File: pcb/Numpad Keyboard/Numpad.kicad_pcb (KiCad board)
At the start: 2 copper layers, 82.4 x 128 mm, 57 parts, among them U1 MCP23S17_SO, U2 IS31FL3743-QF

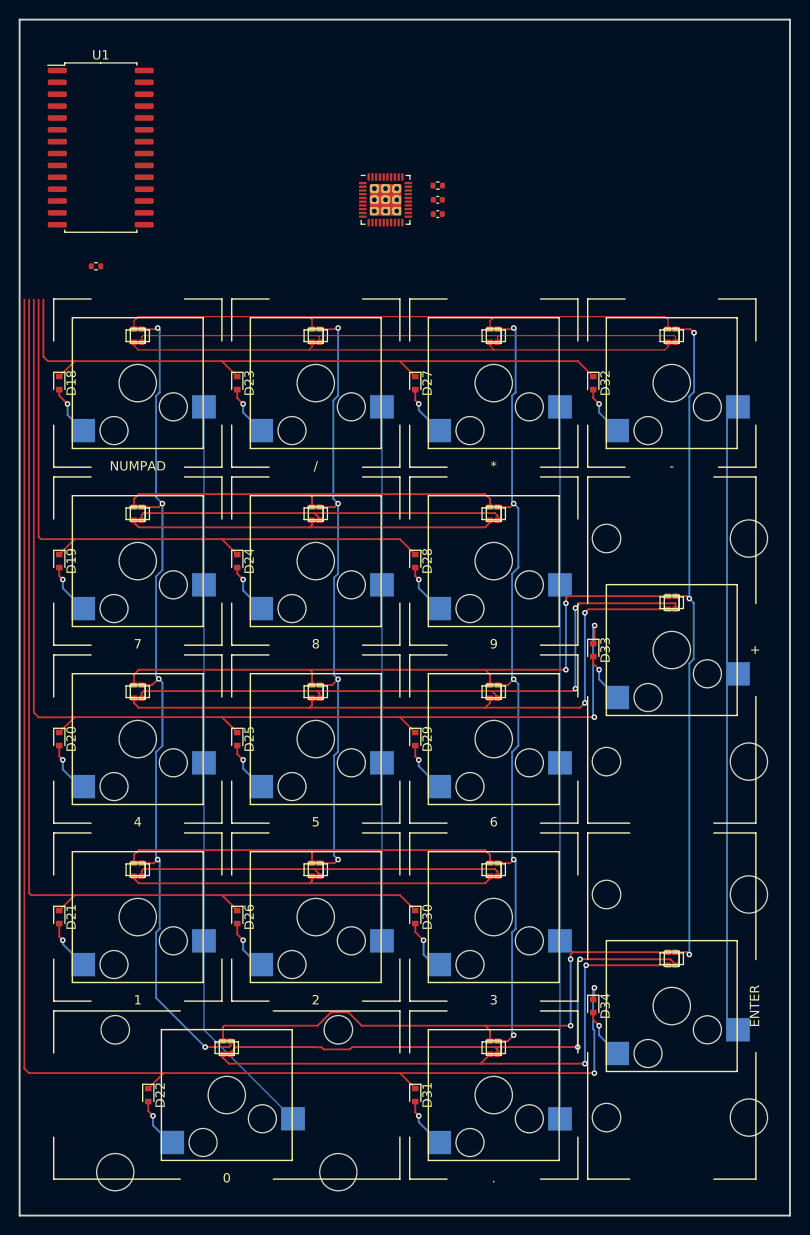
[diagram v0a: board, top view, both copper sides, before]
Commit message: Added second LED controller for higher current per LED
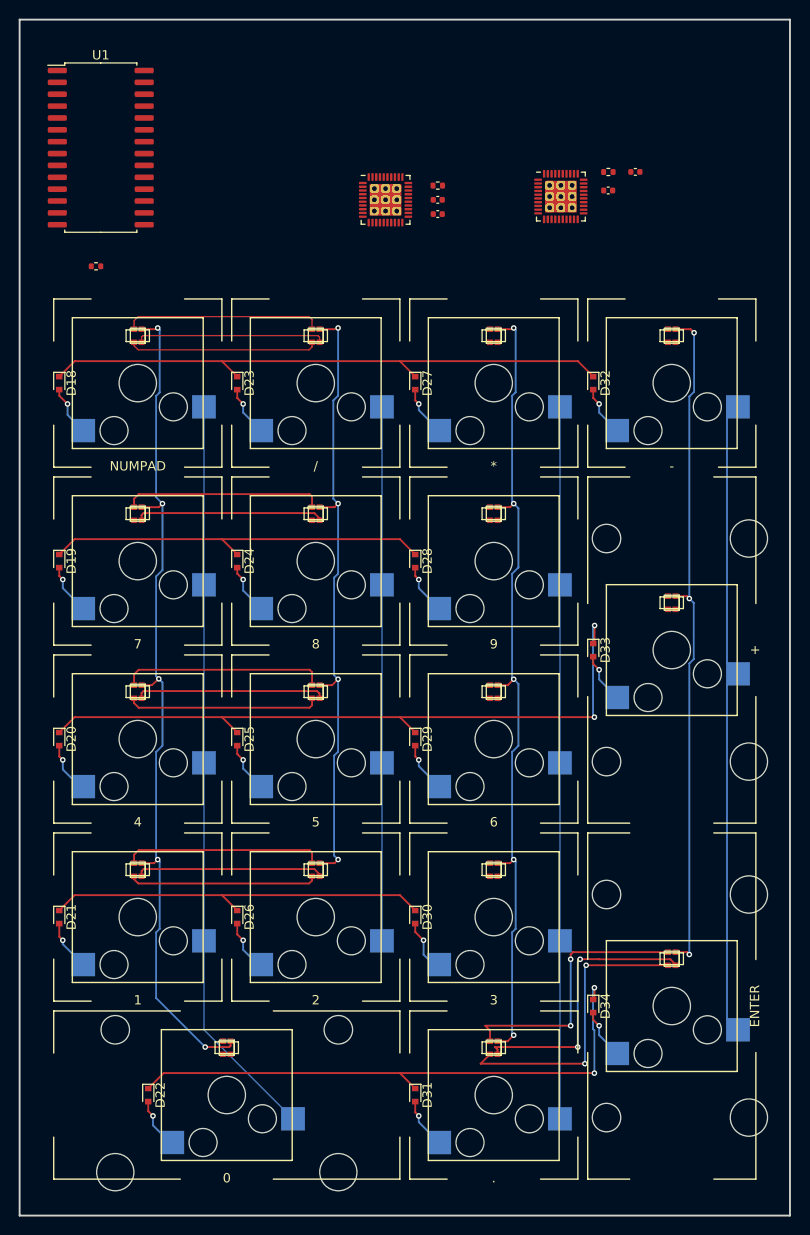
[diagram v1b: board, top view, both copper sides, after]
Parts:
- added C3: C 1uF, Footprints:C_0402_1005Metric, F.Cu at (84.8, 41.1)
- added C4: C_100nF, Footprints:C_0402_1005Metric, F.Cu at (87.7, 39.2)
- added R3: R, Footprints:R_0402_1005Metric, F.Cu at (84.9, 39.2)
- added U3: IS31FL3743-QF, Footprints:QFN-40-1EP_5x5mm_P0.4mm_EP3.4x3.4mm, F.Cu at (79.8, 41.8)
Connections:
- C1 pad 1: Net-(C1-Pad1) -> Net-(R1-Pad1)
- C1 pad 2: Net-(C1-Pad2) -> Net-(R2-Pad1)
- C2 pad 1: Net-(C1-Pad1) -> Net-(R1-Pad1)
- C2 pad 2: Net-(C1-Pad2) -> Net-(R2-Pad1)
- D10 pad 1: Net-(D1-Pad1) -> Net-(D10-Pad1)
- D10 pad 2: Net-(D1-Pad2) -> Net-(D10-Pad2)
- D10 pad 4: Net-(D1-Pad4) -> Net-(D10-Pad4)
- D14 pad 2: Net-(D14-Pad2) -> Net-(D17-Pad2)
- D15 pad 1: Net-(D1-Pad1) -> Net-(D10-Pad1)
- D15 pad 2: Net-(D1-Pad2) -> Net-(D10-Pad2)
- D15 pad 4: Net-(D1-Pad4) -> Net-(D10-Pad4)
- D17 pad 2: Net-(D14-Pad2) -> Net-(D17-Pad2)
- D2 pad 1: Net-(D11-Pad1) -> Net-(D2-Pad1)
- D2 pad 2: Net-(D11-Pad2) -> Net-(D2-Pad2)
- D2 pad 4: Net-(D11-Pad4) -> Net-(D2-Pad4)
- D3 pad 1: Net-(D12-Pad1) -> Net-(D3-Pad1)
- D3 pad 2: Net-(D12-Pad2) -> Net-(D3-Pad2)
- D3 pad 4: Net-(D12-Pad4) -> Net-(D3-Pad4)
- D4 pad 1: Net-(D13-Pad1) -> Net-(D4-Pad1)
- D4 pad 2: Net-(D13-Pad2) -> Net-(D4-Pad2)
- D4 pad 4: Net-(D13-Pad4) -> Net-(D4-Pad4)
- D5 pad 1: Net-(D14-Pad1) -> Net-(D5-Pad1)
- D5 pad 2: Net-(D14-Pad2) -> Net-(D5-Pad2)
- D5 pad 4: Net-(D14-Pad4) -> Net-(D5-Pad4)
- D7 pad 1: Net-(D11-Pad1) -> Net-(D2-Pad1)
- D7 pad 2: Net-(D11-Pad2) -> Net-(D2-Pad2)
- D7 pad 4: Net-(D11-Pad4) -> Net-(D2-Pad4)
- D8 pad 1: Net-(D12-Pad1) -> Net-(D3-Pad1)
- D8 pad 2: Net-(D12-Pad2) -> Net-(D3-Pad2)
- D8 pad 4: Net-(D12-Pad4) -> Net-(D3-Pad4)
- D9 pad 1: Net-(D13-Pad1) -> Net-(D4-Pad1)
- D9 pad 2: Net-(D13-Pad2) -> Net-(D4-Pad2)
- D9 pad 4: Net-(D13-Pad4) -> Net-(D4-Pad4)
- R1 pad 1: Net-(C1-Pad2) -> Net-(R1-Pad1)
- R2 pad 1: Net-(C1-Pad1) -> Net-(R2-Pad1)
- U1 pad 10: Net-(C1-Pad1) -> Net-(R2-Pad1)
- U1 pad 15: Net-(C1-Pad1) -> Net-(R2-Pad1)
- U1 pad 16: Net-(C1-Pad2) -> Net-(R1-Pad1)
- U1 pad 17: Net-(C1-Pad2) -> Net-(R1-Pad1)
- U1 pad 9: Net-(C1-Pad2) -> Net-(R1-Pad1)
- U2 pad 15: Net-(D14-Pad1) -> Net-(D5-Pad1)
- U2 pad 16: Net-(C1-Pad1) -> Net-(R2-Pad1)
- U2 pad 17: Net-(D14-Pad2) -> Net-(D5-Pad2)
- U2 pad 18: Net-(D14-Pad4) -> Net-(D5-Pad4)
- U2 pad 19: Net-(D13-Pad1) -> Net-(D4-Pad1)
- U2 pad 20: Net-(D13-Pad2) -> Net-(D4-Pad2)
- U2 pad 21: Net-(D13-Pad4) -> Net-(D4-Pad4)
- U2 pad 22: Net-(C1-Pad2) -> Net-(R1-Pad1)
- U2 pad 23: Net-(C1-Pad1) -> Net-(R2-Pad1)
- U2 pad 24: Net-(C1-Pad2) -> Net-(R1-Pad1)
- U2 pad 25: Net-(C1-Pad2) -> Net-(R1-Pad1)
- U2 pad 26: Net-(C1-Pad2) -> Net-(R1-Pad1)
- U2 pad 3: Net-(D15-Pad3) -> unconnected-(U2-Pad3)
- U2 pad 31: Net-(D12-Pad1) -> Net-(D3-Pad1)
- U2 pad 32: Net-(D12-Pad2) -> Net-(D3-Pad2)
- U2 pad 33: Net-(D12-Pad4) -> Net-(D3-Pad4)
- U2 pad 34: Net-(D11-Pad1) -> Net-(D2-Pad1)
- U2 pad 35: Net-(D11-Pad2) -> Net-(D2-Pad2)
- U2 pad 36: Net-(D11-Pad4) -> Net-(D2-Pad4)
- U2 pad 5: Net-(C1-Pad2) -> Net-(R1-Pad1)
- U2 pad 7: Net-(D10-Pad3) -> unconnected-(U2-Pad7)
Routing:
- net Net-(D22-Pad1): track 158.7 -> 61.2 mm
- net Net-(D12-Pad2): track 70.2 -> 0.00 mm, vias 2 -> 0
- net Net-(D12-Pad1): track 69.9 -> 0.00 mm, vias 2 -> 0
- net Net-(D12-Pad4): track 69.3 -> 0.00 mm, vias 2 -> 0
- net Net-(D21-Pad1): track 110.3 -> 41.8 mm
- net Net-(D14-Pad2): track 60.1 -> 0.00 mm, vias 2 -> 0
- net Net-(D20-Pad1): track 123.5 -> 74.3 mm
- net Net-(D11-Pad1): track 41.8 -> 0.00 mm
- net Net-(D13-Pad1): track 41.8 -> 0.00 mm
- net Net-(D1-Pad1): track 62.4 -> 21.3 mm
- net Net-(D13-Pad4): track 40.4 -> 0.00 mm
- net Net-(D11-Pad4): track 40.4 -> 0.00 mm
- net Net-(D1-Pad2): track 60.3 -> 20.2 mm
- net Net-(D11-Pad2): track 39.9 -> 0.00 mm
- net Net-(D13-Pad2): track 39.9 -> 0.00 mm
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
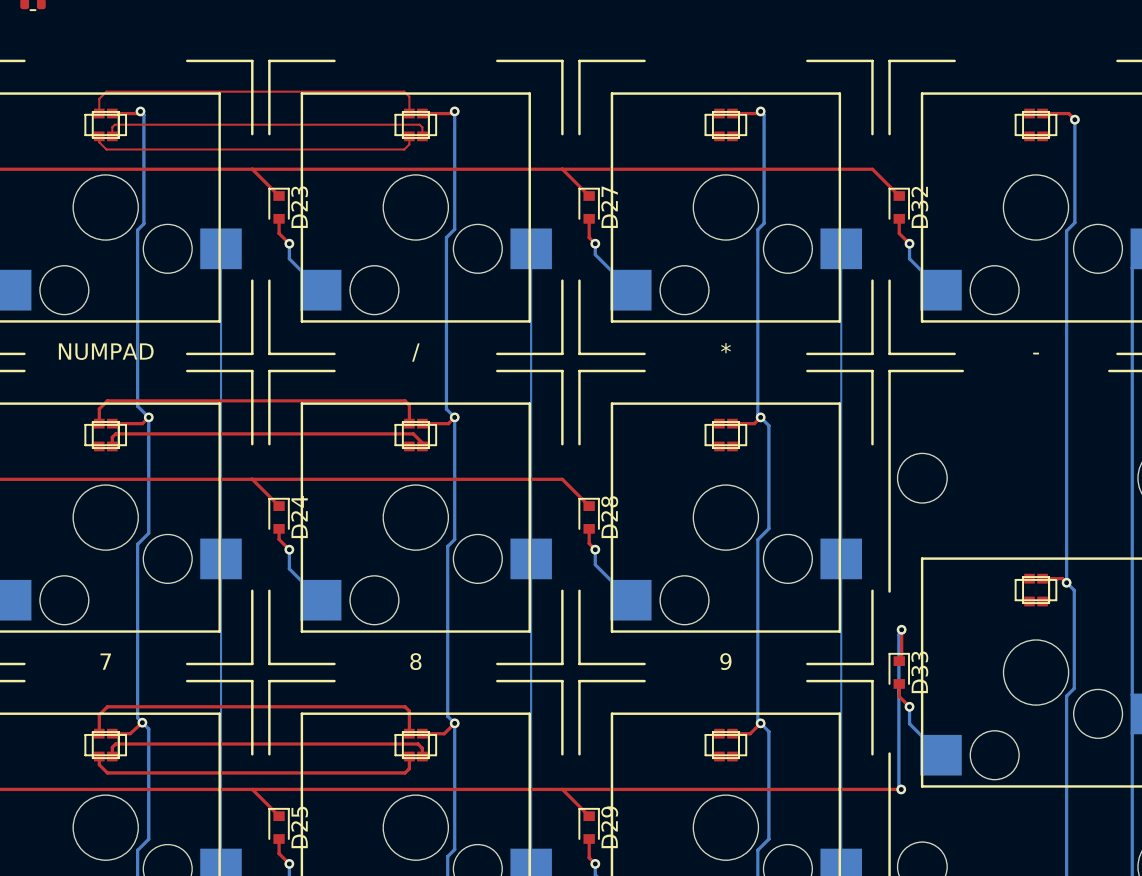
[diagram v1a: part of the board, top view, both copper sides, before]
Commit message: Removed several capacitors to decrease current consumption on startup
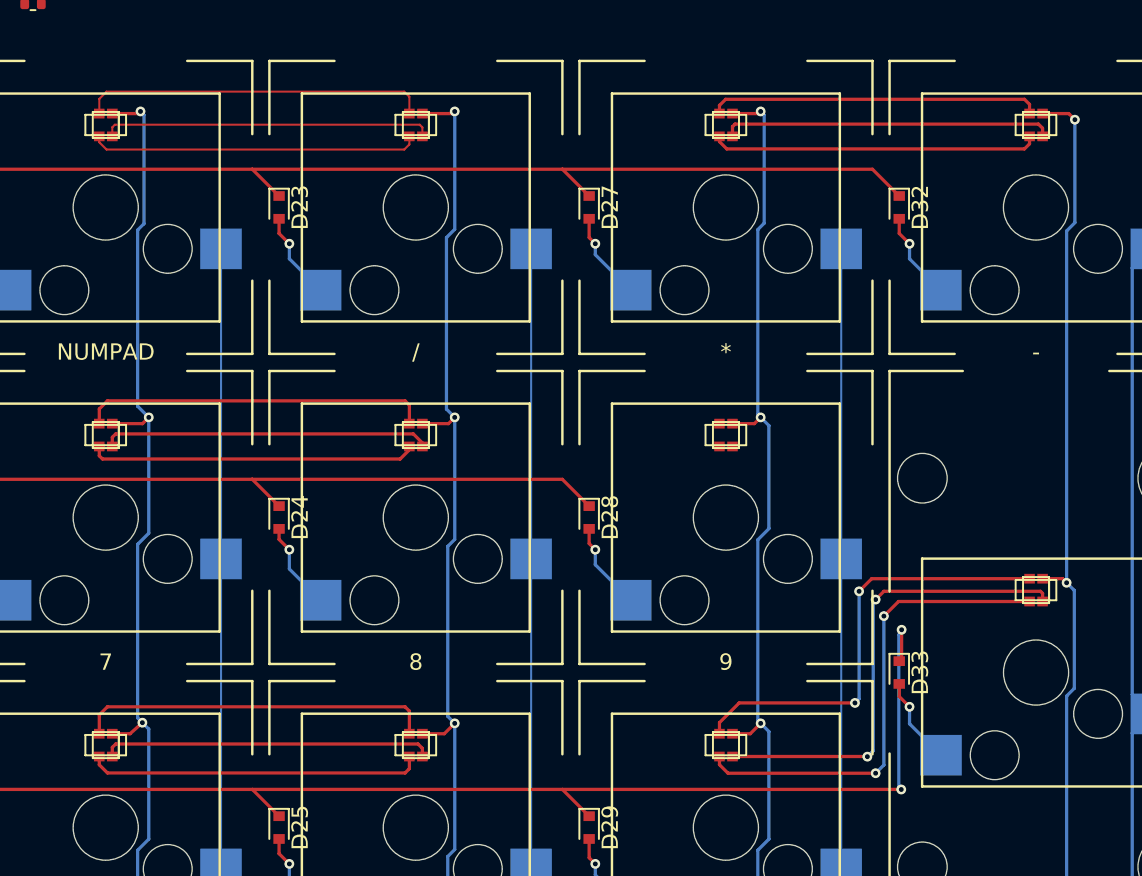
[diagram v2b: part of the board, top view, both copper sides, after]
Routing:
- net Net-(D12-Pad2): track 0.00 -> 29.5 mm, vias 0 -> 2
- net Net-(D12-Pad4): track 0.00 -> 29.2 mm, vias 0 -> 2
- net Net-(D12-Pad1): track 0.00 -> 27.3 mm, vias 0 -> 2
- net Net-(D10-Pad1): track 0.00 -> 20.4 mm
- net Net-(D10-Pad4): track 0.00 -> 20.3 mm
- net Net-(D2-Pad2): track 0.00 -> 20.1 mm
- net Net-(D10-Pad2): track 0.00 -> 20.1 mm
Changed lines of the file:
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@@
   (segment (start 52.882 73.644) (end 53.144 73.906) (width 0.2) (layer "F.Cu") (net 29))
   (segment (start 34.094 75.045) (end 34.094 74.144) (width 0.2) (layer "F.Cu") (net 29))
+  (segment (start 34.094 76.445) (end 34.094 77.02) (width 0.2) (layer "F.Cu") (net 30))
+  (segment (start 34.29 77.216) (end 52.578 77.216) (width 0.2) (layer "F.Cu") (net 30))
+  (segment (start 34.094 77.02) (end 34.29 77.216) (width 0.2) (layer "F.Cu") (net 30))
+  (segment (start 53.144 76.65) (end 53.144 76.445) (width 0.2) (layer "F.Cu") (net 30))
+  (segment (start 52.578 77.216) (end 53.144 76.65) (width 0.2) (layer "F.Cu") (net 30))
   (segment (start 35.102 75.676) (end 53.39 75.676) (width 0.2) (layer "F.Cu") (net 31))
   (segment (start 53.39 75.676) (end 53.944 76.23) (width 0.2) (layer "F.Cu") (net 31))
@@
   (segment (start 34.094 55.995) (end 34.094 55.094) (width 0.127) (layer "F.Cu") (net 46))
   (segment (start 52.828 54.648) (end 53.144 54.964) (width 0.127) (layer "F.Cu") (net 46))
+  (segment (start 82.296 85.344) (end 81.788 85.852) (width 0.2) (layer "F.Cu") (net 50))
+  (segment (start 81.271 95.495) (end 72.994 95.495) (width 0.2) (layer "F.Cu") (net 50))
+  (segment (start 92.044 85.97) (end 92.044 85.47) (width 0.2) (layer "F.Cu") (net 50))
+  (segment (start 81.28 95.504) (end 81.271 95.495) (width 0.2) (layer "F.Cu") (net 50))
+  (segment (start 92.044 85.47) (end 91.918 85.344) (width 0.2) (layer "F.Cu") (net 50))
+  (segment (start 91.918 85.344) (end 82.296 85.344) (width 0.2) (layer "F.Cu") (net 50))
+  (via (at 81.788 85.852) (size 0.6) (drill 0.3) (layers "F.Cu" "B.Cu") (net 50))
+  (via (at 81.28 95.504) (size 0.6) (drill 0.3) (layers "F.Cu" "B.Cu") (net 50))
+  (segment (start 81.642489 85.997511) (end 81.642489 95.141511) (width 0.2) (layer "B.Cu") (net 50))
+  (segment (start 81.788 85.852) (end 81.642489 85.997511) (width 0.2) (layer "B.Cu") (net 50))
+  (segment (start 81.642489 95.141511) (end 81.28 95.504) (width 0.2) (layer "B.Cu") (net 50))
+  (segment (start 72.719 96.52) (end 72.194 95.995) (width 0.2) (layer "F.Cu") (net 51))
+  (segment (start 83.194 85.97) (end 82.296 86.868) (width 0.2) (layer "F.Cu") (net 51))
+  (segment (start 91.244 85.97) (end 83.194 85.97) (width 0.2) (layer "F.Cu") (net 51))
+  (segment (start 72.194 95.995) (end 72.194 95.495) (width 0.2) (layer "F.Cu") (net 51))
+  (segment (start 81.788 96.52) (end 72.719 96.52) (width 0.2) (layer "F.Cu") (net 51))
+  (via (at 81.788 96.52) (size 0.6) (drill 0.3) (layers "F.Cu" "B.Cu") (net 51))
+  (via (at 82.296 86.868) (size 0.6) (drill 0.3) (layers "F.Cu" "B.Cu") (net 51))
+  (segment (start 82.296 86.868) (end 82.296 96.012) (width 0.2) (layer "B.Cu") (net 51))
+  (segment (start 82.296 96.012) (end 81.788 96.52) (width 0.2) (layer "B.Cu") (net 51))
+  (segment (start 72.194 94.095) (end 72.194 93.414) (width 0.2) (layer "F.Cu") (net 52))
+  (segment (start 73.406 92.202) (end 80.518 92.202) (width 0.2) (layer "F.Cu") (net 52))
+  (segment (start 91.244 84.57) (end 81.546 84.57) (width 0.2) (layer "F.Cu") (net 52))
+  (segment (start 72.194 93.414) (end 73.406 92.202) (width 0.2) (layer "F.Cu") (net 52))
+  (segment (start 81.546 84.57) (end 80.772 85.344) (width 0.2) (layer "F.Cu") (net 52))
+  (via (at 80.772 85.344) (size 0.6) (drill 0.3) (layers "F.Cu" "B.Cu") (net 52))
+  (via (at 80.518 92.202) (size 0.6) (drill 0.3) (layers "F.Cu" "B.Cu") (net 52))
+  (segment (start 80.772 85.344) (end 80.772 91.948) (width 0.2) (layer "B.Cu") (net 52))
+  (segment (start 80.772 91.948) (end 80.518 92.202) (width 0.2) (layer "B.Cu") (net 52))
   (segment (start 52.882 96.504) (end 53.144 96.242) (width 0.2) (layer "F.Cu") (net 54))
   (segment (start 34.594 96.504) (end 52.882 96.504) (width 0.2) (layer "F.Cu") (net 54))
@@
   (segment (start 35.102 113.776) (end 53.39 113.776) (width 0.2) (layer "F.Cu") (net 78))
   (segment (start 53.39 113.776) (end 53.944 114.33) (width 0.2) (layer "F.Cu") (net 78))
+  (segment (start 91.244 55.995) (end 91.244 55.43) (width 0.2) (layer "F.Cu") (net 82))
+  (segment (start 72.571 55.118) (end 72.194 55.495) (width 0.2) (layer "F.Cu") (net 82))
+  (segment (start 91.244 55.43) (end 90.932 55.118) (width 0.2) (layer "F.Cu") (net 82))
+  (segment (start 72.194 55.495) (end 72.194 55.995) (width 0.2) (layer "F.Cu") (net 82))
+  (segment (start 90.932 55.118) (end 72.571 55.118) (width 0.2) (layer "F.Cu") (net 82))
+  (segment (start 72.194 57.395) (end 72.194 57.716) (width 0.2) (layer "F.Cu") (net 83))
+  (segment (start 72.194 57.716) (end 72.644 58.166) (width 0.2) (layer "F.Cu") (net 83))
+  (segment (start 72.644 58.166) (end 90.932 58.166) (width 0.2) (layer "F.Cu") (net 83))
+  (segment (start 90.932 58.166) (end 91.244 57.854) (width 0.2) (layer "F.Cu") (net 83))
+  (segment (start 91.244 57.854) (end 91.244 57.395) (width 0.2) (layer "F.Cu") (net 83))
+  (segment (start 73.152 56.642) (end 91.791 56.642) (width 0.2) (layer "F.Cu") (net 84))
+  (segment (start 72.994 57.395) (end 72.994 56.8) (width 0.2) (layer "F.Cu") (net 84))
+  (segment (start 72.994 56.8) (end 73.152 56.642) (width 0.2) (layer "F.Cu") (net 84))
+  (segment (start 91.791 56.642) (end 92.044 56.895) (width 0.2) (layer "F.Cu") (net 84))
+  (segment (start 92.044 56.895) (end 92.044 57.395) (width 0.2) (layer "F.Cu") (net 84))
   (segment (start 71.185 134.604) (end 72.194 133.595) (width 0.2) (layer "F.Cu") (net 85))
   (segment (start 71.185 134.604) (end 82.346 134.604) (width 0.2) (layer "F.Cu") (net 85))
